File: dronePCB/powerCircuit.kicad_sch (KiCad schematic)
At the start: 83 parts, among them IC1 STUSB4500QTR, IC2 MP2338GTL-Z, J3 103AT-2 10k, J4 XT30, J5 JST, SW3 SW_CHG_RST, U4 BQ25792RQMR, U5 NCP1117-3.3_SOT223, U6 BQ76920PW

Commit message: Added micro SD, GPS, magnetometer, gimbal, DVR, Strobes and ToF sensors
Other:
- company: (none) -> Author: Mejpek
- title: (none) -> Power Circuit

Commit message: Added strobe PCB
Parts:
- C26, C33, C39, C46, C47, C62, C63, C64: value 0.1u -> 100n
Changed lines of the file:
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@@
 			)
 		)
-		(property "Value" "0.1u"
+		(property "Value" "100n"
 			(at 48.514 175.514 0)
 			(effects
@@
 			)
 		)
-		(property "Value" "0.1u"
-			(at 201.422 59.944 0)
+		(property "Value" "100n"
+			(at 202.184 60.198 0)
 			(effects
 				(font
@@
 			)
 		)
-		(property "Value" "0.1u"
+		(property "Value" "100n"
 			(at 248.666 34.29 90)
 			(effects
@@
 			)
 		)
-		(property "Value" "0.1u"
+		(property "Value" "100n"
 			(at 177.038 22.606 0)
 			(effects
@@
 			)
 		)
-		(property "Value" "0.1u"
-			(at 236.474 34.29 90)
+		(property "Value" "100n"
+			(at 236.982 34.29 90)
 			(effects
 				(font
@@
 			)
 		)
-		(property "Value" "0.1u"
-			(at 215.392 78.994 0)
+		(property "Value" "100n"
+			(at 216.154 78.994 0)
 			(effects
 				(font
@@
 			)
 		)
-		(property "Value" "0.1u"
-			(at 92.71 171.45 90)
+		(property "Value" "100n"
+			(at 92.456 171.45 90)
 			(effects
 				(font
@@
 			)
 		)
-		(property "Value" "0.1u"
+		(property "Value" "100n"
 			(at 260.096 34.29 90)
 			(effects

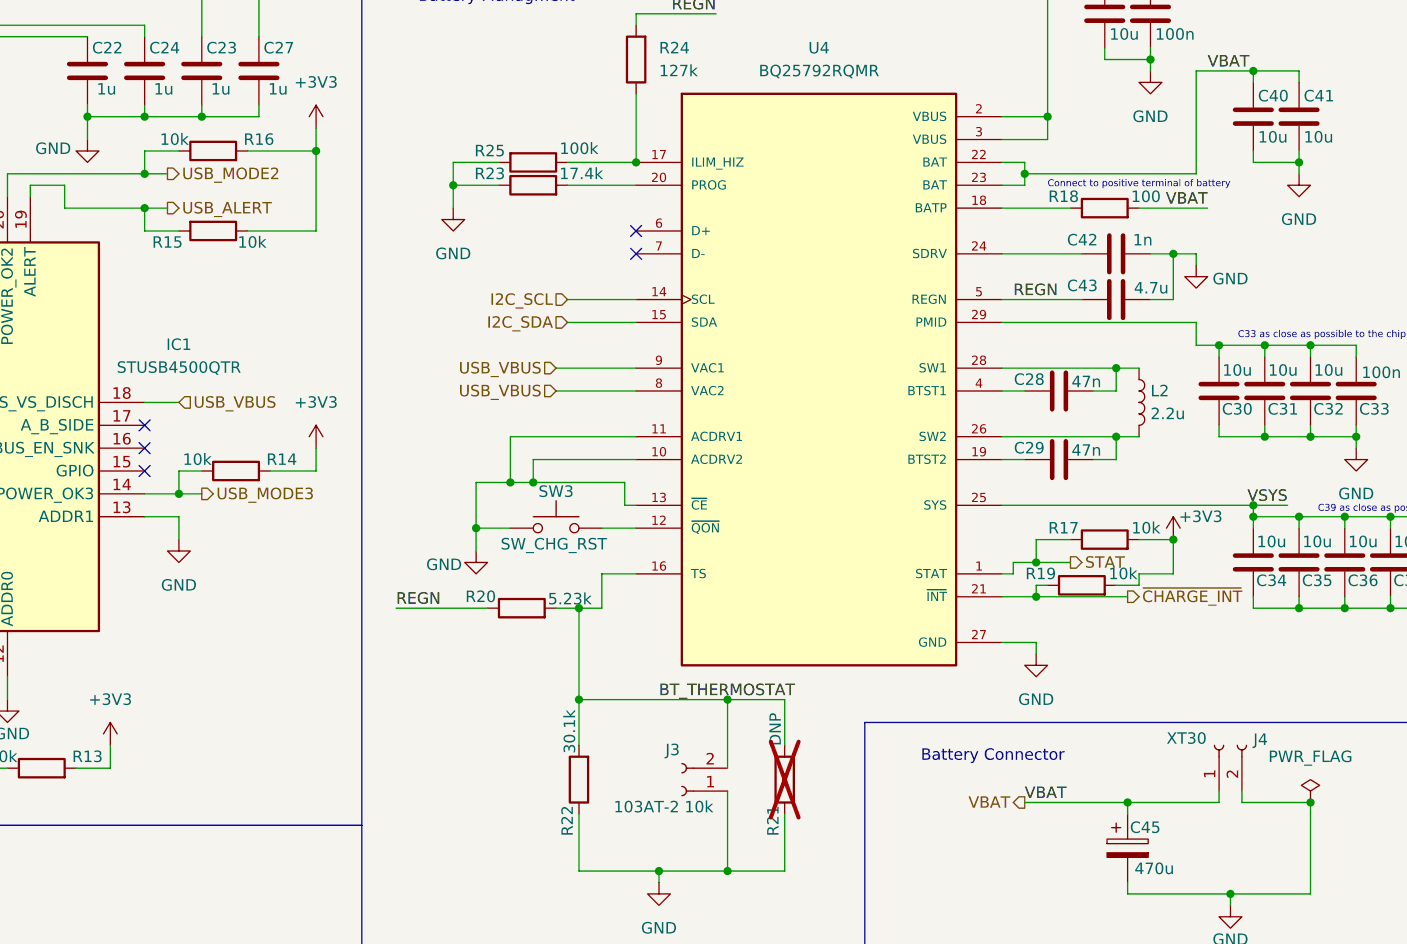
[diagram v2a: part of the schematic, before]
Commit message: Routed RP2350B w/ dependencies + power circuit
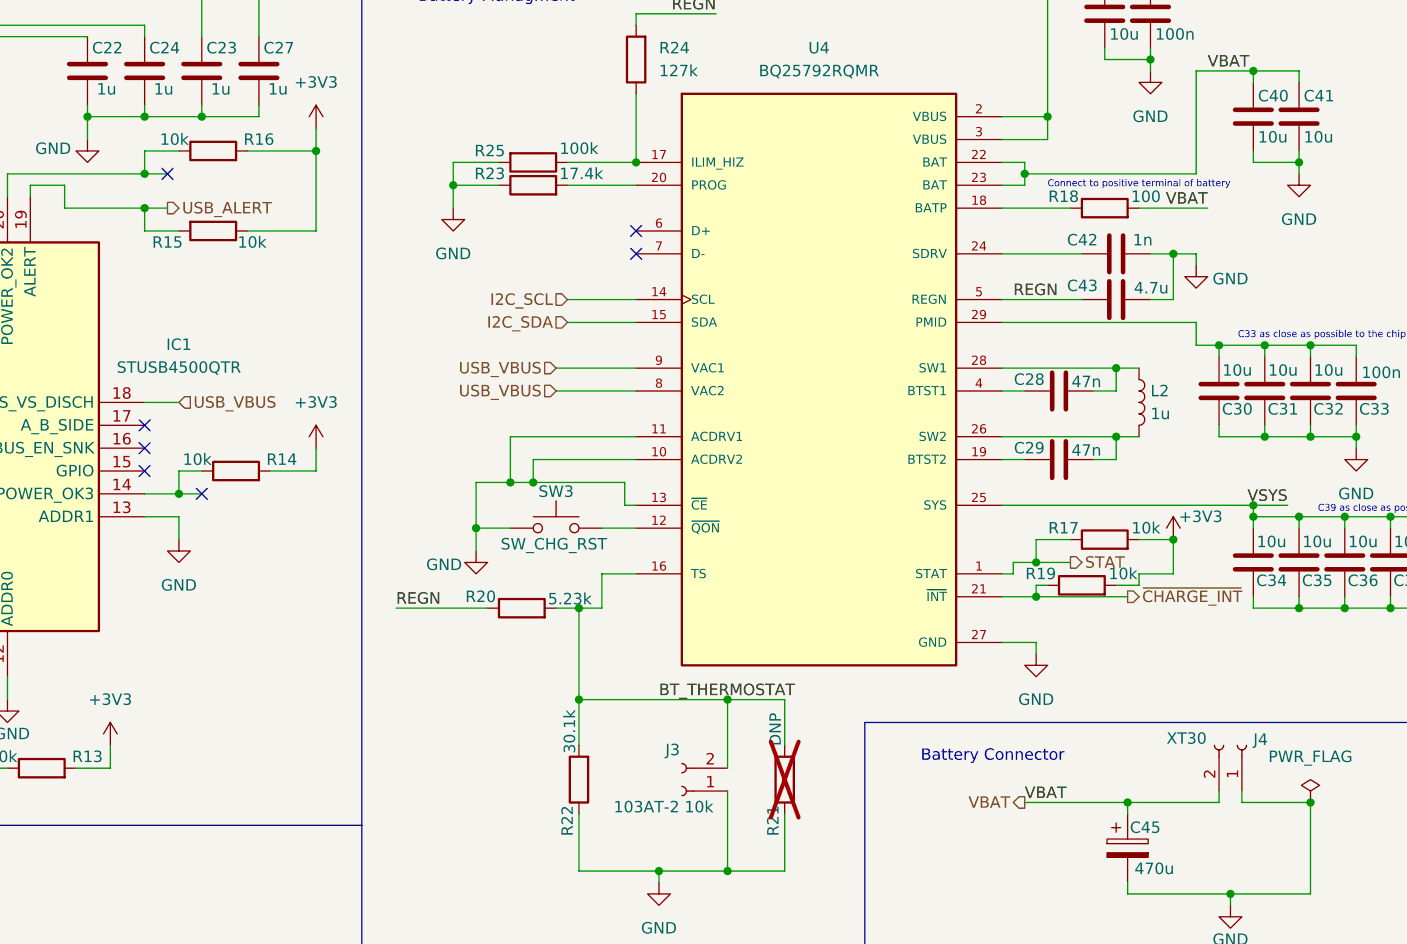
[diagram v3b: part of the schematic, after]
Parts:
- C22, C23, C24, C25, C26, C27, C28, C29, C30, C31, C32, C33, C34, C35, C36, C37, C38, C39, C40, C41, C42, C43, C44, C46, C47, C48, C49, C50, C51, C52, C53, C54, C55, C56, C57, C58, C59, C60, C61, C62, C63, C64, C65, R13, R14, R15, R16, R17, R18, R19, R20, R21, R22, R23, R24, R25, R26, R27, R28, R29, R30, R31, R32, R33, R34, R36, R37, R38, R39, R40, R41: footprint (none) -> Capacitor_SMD:C_0805_2012Metric_Pad1.18x1.45mm_HandSolder
- C45: footprint (none) -> Capacitor_SMD:C_Elec_3x5.4
- IC1: footprint QFN50P400X400X100-25N-D -> droneParts:STUSB4500QTR
- IC2: footprint MP2338GTLZ -> droneParts:MP2338GTLZ
- J3: footprint (none) -> Connector_JST:JST_PH_B2B-PH-SM4-TB_1x02-1MP_P2.00mm_Vertical
- J4: footprint (none) -> Connector_AMASS:AMASS_XT30U-F_1x02_P5.0mm_Vertical
- J5: footprint (none) -> Connector_JST:JST_PH_B5B-PH-SM4-TB_1x05-1MP_P2.00mm_Vertical
- L2: value 2.2u -> 1u; footprint (none) -> droneParts:AMPLH7020S-1R0MT
- L3: footprint (none) -> droneParts:AMPLH5030S-6R8MT
- SW3: footprint (none) -> Button_Switch_SMD:SW_Push_1P1T_NO_Vertical_Wuerth_434133025816
- U4: footprint BQ25792RQMR:QFN40P400X400X100-29N -> droneParts:BQ25792RQMR
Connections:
- net GND: now also J4.1 (Pin_2); no longer J4.2 (Pin_2)
- net VBAT: now also J4.2 (Pin_1); no longer J4.1 (Pin_1)
- net USB_MODE2: no longer names the net of IC1.20 (POWER_OK2), R16.1
- net USB_MODE3: no longer names the net of IC1.14 (POWER_OK3), R14.1
- no-connect marks 8 -> 10
